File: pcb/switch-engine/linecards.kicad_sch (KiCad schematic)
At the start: 11 parts, among them J14 ARF6-08-S-D-A-K-TR, J15 ARF6-08-S-D-A-K-TR, J16 CONN_01X10, J17 ARF6-08-S-D-A-K-TR, J18 ARF6-08-S-D-A-K-TR, J19 CONN_01X10, U15 SIT9121AI-2BF-XXS156.250000G, U8 XILINX_ULTRASCALEPLUS_B676

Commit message: Continued initial schematic work on switch engine
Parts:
- added C104, C105, C106, C107, C108, C109, C110, C98: 0.47 uF, azonenberg_pcb:EIA_0402_CAP_NOSILK, symbol device:C
- added U18, U19, U20, U21: 74LVC1T45, azonenberg_pcb:DFN_6_0.5MM_1.6x1.6MM_TI_DPK, symbol special-azonenberg:74LVC1T45
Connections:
- net 2V5: now also C107.1, C108.1, C109.1, C110.1, U18.6 (VCCB), U19.6 (VCCB), U20.6 (VCCB), U21.6 (VCCB)
- net 3V3: now also C104.1, C105.1, C106.1, C98.1, U18.1 (VCCA), U19.1 (VCCA), U20.1 (VCCA), U21.1 (VCCA)
- net GND: now also C104.2, C105.2, C106.2, C107.2, C108.2, C109.2, C110.2, C98.2, U18.2 (GND), U19.2 (GND), U20.2 (GND), U21.2 (GND)
- net LC0_MDC: now also U20.4 (B)
- net LC0_MDC_3V3: now also U20.3 (A)
- net LC0_MDIO: now also U18.4 (B)
- net LC0_MDIO_3V3: now also U18.3 (A)
- net LC0_MDIO_OE: now also U18.5 (DIR)
- net LC1_MDC: now also U21.4 (B)
- net LC1_MDC_3V3: now also U21.3 (A)
- net LC1_MDIO: now also U19.4 (B)
- net LC1_MDIO_3V3: now also U19.3 (A)
- net LC1_MDIO_OE: now also U19.5 (DIR)
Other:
- note added: "MDIO/MDC to line cards are LVCMOS25 Everything else is LVCMOS33"
- note removed: "NOTE: MDIO/MDC to line cards are LVCMOS25 Everything else is LVCMOS33"

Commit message: First iteration of main board PCB schematic is now passing ERC
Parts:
- U8: value XILINX_ULTRASCALEPLUS_B676 -> XCKU5P-2FFVB676I
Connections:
- net 3V3: now also U20.5 (DIR), U21.5 (DIR)
- no-connect marks 24 -> 32
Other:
- company: (none) -> Antikernel Labs
- title: (none) -> LATENTRED Ethernet Switch - Main Board
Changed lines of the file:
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@@
 	(generator_version "8.0")
 	(paper "A3")
+	(title_block
+		(title "LATENTRED Ethernet Switch - Main Board")
+		(date "2025-06-02")
+		(rev "0.1")
+		(company "Antikernel Labs")
+		(comment 1 "Andrew D. Zonenberg")
+	)
 	(junction
 		(at 147.32 205.74)
@@
 	)
 	(no_connect
+		(at 64.77 241.3)
+	)
+	(no_connect
 		(at 39.37 187.96)
 	)
@@
 	)
 	(no_connect
+		(at 147.32 241.3)
+	)
+	(no_connect
+		(at 64.77 190.5)
+	)
+	(no_connect
 		(at 39.37 41.91)
 	)
@@
 	)
 	(no_connect
+		(at 147.32 243.84)
+	)
+	(no_connect
+		(at 147.32 190.5)
+	)
+	(no_connect
 		(at 201.93 193.04)
 	)
@@
 	)
 	(no_connect
+		(at 64.77 243.84)
+	)
+	(no_connect
 		(at 39.37 49.53)
 	)
@@
 	)
 	(no_connect
+		(at 147.32 187.96)
+	)
+	(no_connect
+		(at 64.77 187.96)
+	)
+	(no_connect
 		(at 39.37 241.3)
 	)
@@
 	(wire
 		(pts
+			(xy 298.45 74.93) (xy 298.45 77.47)
+		)
+		(stroke
+			(width 0)
+			(type default)
+		)
+	)
+	(wire
+		(pts
 			(xy 64.77 149.86) (xy 64.77 152.4)
 		)
@@
 	(wire
 		(pts
+			(xy 298.45 58.42) (xy 298.45 60.96)
+		)
+		(stroke
+			(width 0)
+			(type default)
+		)
+	)
+	(wire
+		(pts
 			(xy 121.92 210.82) (xy 121.92 213.36)
 		)
@@
 			)
 		)
-		(property "Value" "XILINX_ULTRASCALEPLUS_B676"
+		(property "Value" "XCKU5P-2FFVB676I"
 			(at 207.01 205.74 0)
 			(effects
@@
 			)
 		)
-		(property "Value" "XILINX_ULTRASCALEPLUS_B676"
+		(property "Value" "XCKU5P-2FFVB676I"
 			(at 207.01 125.73 0)
 			(effects
@@
 			)
 		)
-		(property "Value" "XILINX_ULTRASCALEPLUS_B676"
+		(property "Value" "XCKU5P-2FFVB676I"
 			(at 44.45 125.73 0)
 			(effects
@@
 			)
 		)
-		(property "Value" "XILINX_ULTRASCALEPLUS_B676"
+		(property "Value" "XCKU5P-2FFVB676I"
 			(at 125.73 125.73 0)
 			(effects

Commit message: Added footprints and created initial skeleton of layout
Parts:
- U8: footprint (none) -> azonenberg_pcb:BGA_676_27x27_FULLARRAY_1MM_FFG676
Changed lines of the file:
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@@
 			)
 		)
-		(property "Footprint" ""
+		(property "Footprint" "azonenberg_pcb:BGA_676_27x27_FULLARRAY_1MM_FFG676"
 			(at 270.51 200.66 0)
 			(effects
@@
 			)
 		)
-		(property "Footprint" ""
+		(property "Footprint" "azonenberg_pcb:BGA_676_27x27_FULLARRAY_1MM_FFG676"
 			(at 270.51 120.65 0)
 			(effects
@@
 			)
 		)
-		(property "Footprint" ""
+		(property "Footprint" "azonenberg_pcb:BGA_676_27x27_FULLARRAY_1MM_FFG676"
 			(at 107.95 120.65 0)
 			(effects
@@
 			)
 		)
-		(property "Footprint" ""
+		(property "Footprint" "azonenberg_pcb:BGA_676_27x27_FULLARRAY_1MM_FFG676"
 			(at 189.23 120.65 0)
 			(effects

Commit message: Lots of progress routing ARC6s
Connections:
- net LC0_PHY0_LANE0_TX_N: now also U8.AA5 (MGTYTXP0_225); no longer U8.AA4 (MGTYTXN0_225)
- net LC0_PHY0_LANE0_TX_P: now also U8.AA4 (MGTYTXN0_225); no longer U8.AA5 (MGTYTXP0_225)
- net LC0_PHY0_LANE1_TX_N: now also U8.W5 (MGTYTXP1_225); no longer U8.W4 (MGTYTXN1_225)
- net LC0_PHY0_LANE1_TX_P: now also U8.W4 (MGTYTXN1_225); no longer U8.W5 (MGTYTXP1_225)
- net LC0_PHY0_LANE2_RX_N: now also U8.T2 (MGTYRXP2_225); no longer U8.T1 (MGTYRXN2_225)
- net LC0_PHY0_LANE2_RX_P: now also U8.T1 (MGTYRXN2_225); no longer U8.T2 (MGTYRXP2_225)
- net LC0_PHY0_LANE2_TX_N: now also U8.U5 (MGTYTXP2_225); no longer U8.U4 (MGTYTXN2_225)
- net LC0_PHY0_LANE2_TX_P: now also U8.U4 (MGTYTXN2_225); no longer U8.U5 (MGTYTXP2_225)
- net LC0_PHY1_LANE0_TX_N: now also U8.R5 (MGTYTXP3_225); no longer U8.R4 (MGTYTXN3_225)
- net LC0_PHY1_LANE0_TX_P: now also U8.R4 (MGTYTXN3_225); no longer U8.R5 (MGTYTXP3_225)
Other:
- note added: "Polarity swap"
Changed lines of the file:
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@@
+		)
+	)
+	(text "Polarity swap"
+		(exclude_from_sim no)
+		(at 62.23 95.25 0)
+		(effects
+			(font
+				(size 1.27 1.27)
+			)
+			(justify left)
+		)
+	)
+	(text "Polarity swap"
+		(exclude_from_sim no)
+		(at 62.23 82.55 0)
+		(effects
+			(font
+				(size 1.27 1.27)
+			)
+			(justify left)
+		)
+	)
+	(text "Polarity swap"
+		(exclude_from_sim no)
+		(at 60.96 118.11 0)
+		(effects
+			(font
+				(size 1.27 1.27)
+			)
+			(justify left)
 		)
 	)
@@
 		)
 	)
+	(text "Polarity swap"
+		(exclude_from_sim no)
+		(at 62.23 102.87 0)
+		(effects
+			(font
+				(size 1.27 1.27)
+			)
+			(justify left)
+		)
+	)
 	(text "Line card 1"
 		(exclude_from_sim no)
@@
 		)
 	)
+	(text "Polarity swap"
+		(exclude_from_sim no)
+		(at 62.23 110.49 0)
+		(effects
+			(font
+				(size 1.27 1.27)
+			)
+			(justify left)
+		)
+	)
 	(label "LC0_PHY0_LANE2_RX_P"
-		(at 39.37 80.01 180)
+		(at 39.37 82.55 180)
 		(fields_autoplaced yes)
 		(effects
@@
 	)
 	(label "LC0_PHY0_LANE2_TX_N"
-		(at 39.37 113.03 180)
+		(at 39.37 110.49 180)
 		(fields_autoplaced yes)
 		(effects
@@
 	)
 	(label "LC0_PHY0_LANE1_TX_N"
-		(at 39.37 105.41 180)
+		(at 39.37 102.87 180)
 		(fields_autoplaced yes)
 		(effects
@@
 	)
 	(label "LC0_PHY0_LANE1_TX_P"
-		(at 39.37 102.87 180)
+		(at 39.37 105.41 180)
 		(fields_autoplaced yes)
 		(effects
@@
 	)
 	(label "LC0_PHY1_LANE0_TX_P"
-		(at 39.37 118.11 180)
+		(at 39.37 120.65 180)
 		(fields_autoplaced yes)
 		(effects
@@
 	)
 	(label "LC0_PHY0_LANE2_RX_N"
-		(at 39.37 82.55 180)
+		(at 39.37 80.01 180)
 		(fields_autoplaced yes)
 		(effects
@@
 	)
 	(label "LC0_PHY1_LANE0_TX_N"
-		(at 39.37 120.65 180)
+		(at 39.37 118.11 180)
 		(fields_autoplaced yes)
 		(effects
@@
 	)
 	(label "LC0_PHY0_LANE0_TX_N"
-		(at 39.37 97.79 180)
+		(at 39.37 95.25 180)
 		(fields_autoplaced yes)
 		(effects
@@
 	)
 	(label "LC0_PHY0_LANE2_TX_P"
-		(at 39.37 110.49 180)
+		(at 39.37 113.03 180)
 		(fields_autoplaced yes)
 		(effects
@@
 	)
 	(label "LC0_PHY0_LANE0_TX_P"
-		(at 39.37 95.25 180)
-		(fields_autoplaced yes)
-		(effects
+		(at 39.37 97.79 180)
+		(fields_autoplaced yes)
+		(effects

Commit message: Progress on GTY routing
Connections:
- net LC0_PHY1_LANE1_TX_N: now also U8.N5 (MGTYTXP0_226); no longer U8.N4 (MGTYTXN0_226)
- net LC0_PHY1_LANE1_TX_P: now also U8.N4 (MGTYTXN0_226); no longer U8.N5 (MGTYTXP0_226)
- net LC0_PHY1_LANE2_TX_N: now also U8.L5 (MGTYTXP1_226); no longer U8.L4 (MGTYTXN1_226)
- net LC0_PHY1_LANE2_TX_P: now also U8.L4 (MGTYTXN1_226); no longer U8.L5 (MGTYTXP1_226)
- net LC1_PHY0_LANE0_TX_N: now also U8.J5 (MGTYTXP2_226); no longer U8.J4 (MGTYTXN2_226)
- net LC1_PHY0_LANE0_TX_P: now also U8.J4 (MGTYTXN2_226); no longer U8.J5 (MGTYTXP2_226)
- net LC1_PHY0_LANE1_TX_N: now also U8.G5 (MGTYTXP3_226); no longer U8.G4 (MGTYTXN3_226)
- net LC1_PHY0_LANE1_TX_P: now also U8.G4 (MGTYTXN3_226); no longer U8.G5 (MGTYTXP3_226)
- net LC1_PHY0_LANE2_RX_N: now also U8.C3 (MGTYRXN1_227); no longer U8.D1 (MGTYRXN0_227)
- net LC1_PHY0_LANE2_RX_P: now also U8.C4 (MGTYRXP1_227); no longer U8.D2 (MGTYRXP0_227)
- net LC1_PHY0_LANE2_TX_N: now also U8.E5 (MGTYTXP1_227); no longer U8.F6 (MGTYTXN0_227)
- net LC1_PHY0_LANE2_TX_P: now also U8.E4 (MGTYTXN1_227); no longer U8.F7 (MGTYTXP0_227)
- net LC1_PHY1_LANE0_RX_N: now also U8.D1 (MGTYRXN0_227); no longer U8.C3 (MGTYRXN1_227)
- net LC1_PHY1_LANE0_RX_P: now also U8.D2 (MGTYRXP0_227); no longer U8.C4 (MGTYRXP1_227)
- net LC1_PHY1_LANE0_TX_N: now also U8.F6 (MGTYTXN0_227); no longer U8.E4 (MGTYTXN1_227)
- net LC1_PHY1_LANE0_TX_P: now also U8.F7 (MGTYTXP0_227); no longer U8.E5 (MGTYTXP1_227)
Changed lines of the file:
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@@
+		)
+	)
+	(text "Polarity swap"
+		(exclude_from_sim no)
+		(at 223.52 102.87 0)
+		(effects
+			(font
+				(size 1.27 1.27)
+			)
+			(justify left)
 		)
 	)
@@
 		)
 	)
+	(text "Polarity swap"
+		(exclude_from_sim no)
+		(at 142.24 110.49 0)
+		(effects
+			(font
+				(size 1.27 1.27)
+			)
+			(justify left)
+		)
+	)
 	(text "MDIO level shifters"
 		(exclude_from_sim no)
@@
 		)
 	)
+	(text "Polarity swap"
+		(exclude_from_sim no)
+		(at 142.24 95.25 0)
+		(effects
+			(font
+				(size 1.27 1.27)
+			)
+			(justify left)
+		)
+	)
 	(text "Low speed control buses"
 		(exclude_from_sim no)
@@
 		)
 	)
+	(text "Polarity swap"
+		(exclude_from_sim no)
+		(at 142.24 118.11 0)
+		(effects
+			(font
+				(size 1.27 1.27)
+			)
+			(justify left)
+		)
+	)
 	(text "Use ARC6-08-12.0-LU-LD-2-1 cable"
 		(exclude_from_sim no)
@@
 		)
 	)
+	(text "Polarity swap"
+		(exclude_from_sim no)
+		(at 142.24 102.87 0)
+		(effects
+			(font
+				(size 1.27 1.27)
+			)
+			(justify left)
+		)
+	)
 	(text "MDIO/MDC to line cards are LVCMOS25\nEverything else is LVCMOS33"
 		(exclude_from_sim no)
@@
 	)
 	(label "LC1_PHY1_LANE0_RX_P"
-		(at 201.93 72.39 180)
+		(at 201.93 64.77 180)
 		(fields_autoplaced yes)
 		(effects
@@
 	)
 	(label "LC1_PHY0_LANE0_TX_N"
-		(at 120.65 113.03 180)
+		(at 120.65 110.49 180)
 		(fields_autoplaced yes)
 		(effects
@@
 	)
 	(label "LC1_PHY0_LANE0_TX_P"
-		(at 120.65 110.49 180)
+		(at 120.65 113.03 180)
 		(fields_autoplaced yes)
 		(effects
@@
 	)
 	(label "LC1_PHY1_LANE0_TX_P"
-		(at 201.93 102.87 180)
+		(at 201.93 95.25 180)
 		(fields_autoplaced yes)
 		(effects
@@
 	)
 	(label "LC1_PHY0_LANE2_RX_P"
-		(at 201.93 64.77 180)
+		(at 201.93 72.39 180)
 		(fields_autoplaced yes)
 		(effects
@@
 	)
 	(label "LC1_PHY0_LANE1_TX_N"
-		(at 120.65 120.65 180)
+		(at 120.65 118.11 180)
 		(fields_autoplaced yes)
 		(effects
@@
 	)
 	(label "LC1_PHY0_LANE2_TX_N"
-		(at 201.93 97.79 180)
+		(at 201.93 102.87 180)
 		(fields_autoplaced yes)
 		(effects
@@
 	)
 	(label "LC1_PHY1_LANE0_RX_N"
-		(at 201.93 74.93 180)
+		(at 201.93 67.31 180)
 		(fields_autoplaced yes)
 		(effects
@@
 	)
 	(label "LC0_PHY1_LANE1_TX_N"
-		(at 120.65 97.79 180)
+		(at 120.65 95.25 180)
 		(fields_autoplaced yes)
 		(effects
@@
 	)
 	(label "LC0_PHY1_LANE2_TX_N"
-		(at 120.65 105.41 180)
+		(at 120.65 102.87 180)
 		(fields_autoplaced yes)
 		(effects
@@
 	)
 	(label "LC1_PHY0_LANE2_TX_P"
-		(at 201.93 95.25 180)
+		(at 201.93 105.41 180)
 		(fields_autoplaced yes)
 		(effects
@@
 	)
 	(label "LC1_PHY0_LANE1_TX_P"
-		(at 120.65 118.11 180)
+		(at 120.65 120.65 180)
 		(fields_autoplaced yes)
 		(effects
@@
 	)
 	(label "LC1_PHY0_LANE2_RX_N"
-		(at 201.93 67.31 180)
+		(at 201.93 74.93 180)
 		(fields_autoplaced yes)
 		(effects
@@
 	)
 	(label "LC0_PHY1_LANE1_TX_P"
-		(at 120.65 95.25 180)
+		(at 120.65 97.79 180)
 		(fields_autoplaced yes)
 		(effects
@@
 	)
 	(label "LC0_PHY1_LANE2_TX_P"
-		(at 120.65 102.87 180)
+		(at 120.65 105.41 180)
 		(fields_autoplaced yes)
 		(effects
@@
 	)
 	(label "LC1_PHY1_LANE0_TX_N"
-		(at 201.93 105.41 180)
-		(fields_autoplaced yes)
-		(effects
+		(at 201.93 97.79 180)
+		(fields_autoplaced yes)
+		(effects

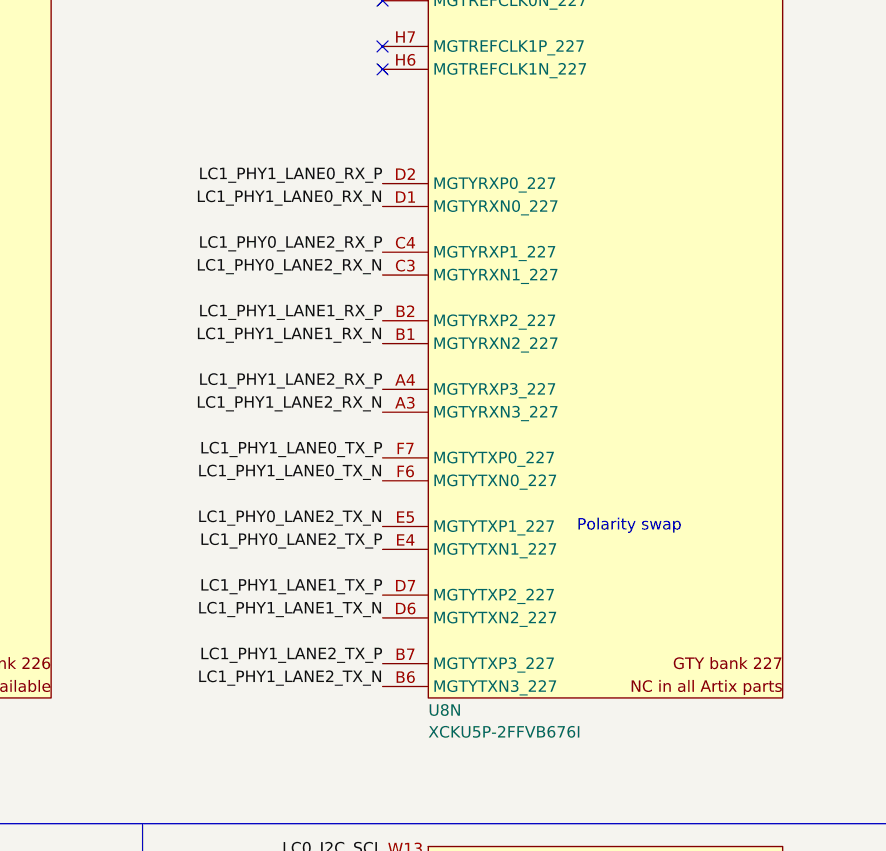
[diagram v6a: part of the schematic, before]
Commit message: More tweaking to SERDES routing
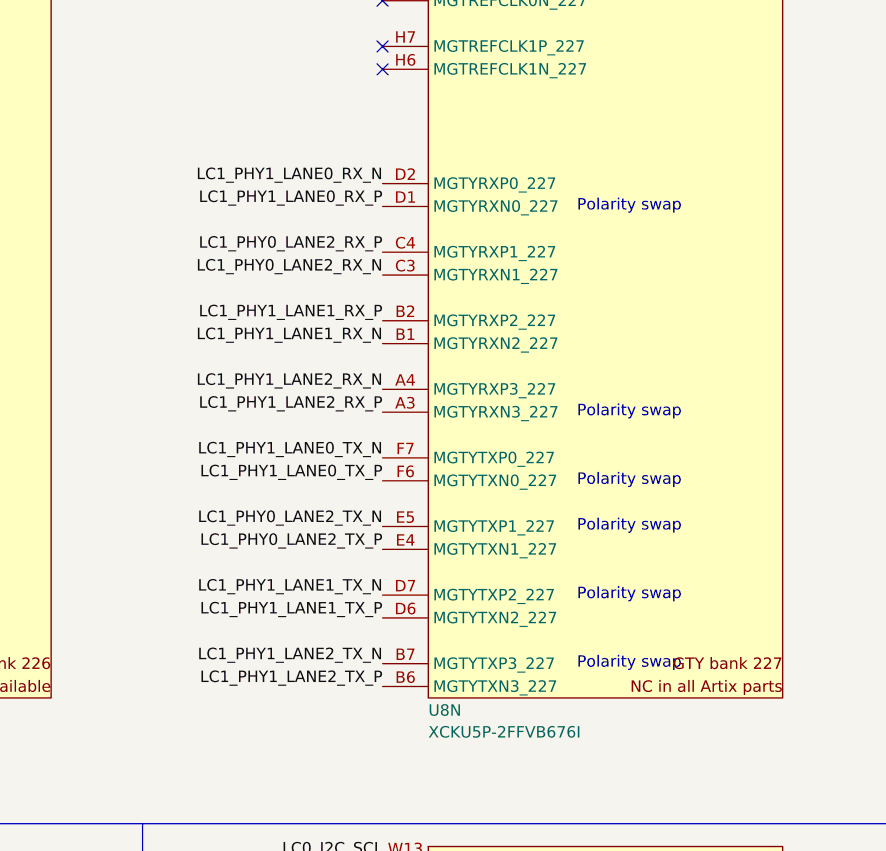
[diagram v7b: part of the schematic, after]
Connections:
- net LC1_PHY1_LANE0_RX_N: now also U8.D2 (MGTYRXP0_227); no longer U8.D1 (MGTYRXN0_227)
- net LC1_PHY1_LANE0_RX_P: now also U8.D1 (MGTYRXN0_227); no longer U8.D2 (MGTYRXP0_227)
- net LC1_PHY1_LANE0_TX_N: now also U8.F7 (MGTYTXP0_227); no longer U8.F6 (MGTYTXN0_227)
- net LC1_PHY1_LANE0_TX_P: now also U8.F6 (MGTYTXN0_227); no longer U8.F7 (MGTYTXP0_227)
- net LC1_PHY1_LANE1_TX_N: now also U8.D7 (MGTYTXP2_227); no longer U8.D6 (MGTYTXN2_227)
- net LC1_PHY1_LANE1_TX_P: now also U8.D6 (MGTYTXN2_227); no longer U8.D7 (MGTYTXP2_227)
- net LC1_PHY1_LANE2_RX_N: now also U8.A4 (MGTYRXP3_227); no longer U8.A3 (MGTYRXN3_227)
- net LC1_PHY1_LANE2_RX_P: now also U8.A3 (MGTYRXN3_227); no longer U8.A4 (MGTYRXP3_227)
- net LC1_PHY1_LANE2_TX_N: now also U8.B7 (MGTYTXP3_227); no longer U8.B6 (MGTYTXN3_227)
- net LC1_PHY1_LANE2_TX_P: now also U8.B6 (MGTYTXN3_227); no longer U8.B7 (MGTYTXP3_227)
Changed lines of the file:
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@@
+		)
+	)
+	(text "Polarity swap"
+		(exclude_from_sim no)
+		(at 223.52 67.31 0)
+		(effects
+			(font
+				(size 1.27 1.27)
+			)
+			(justify left)
 		)
 	)
@@
 	(text "Polarity swap"
 		(exclude_from_sim no)
+		(at 223.52 118.11 0)
+		(effects
+			(font
+				(size 1.27 1.27)
+			)
+			(justify left)
+		)
+	)
+	(text "Polarity swap"
+		(exclude_from_sim no)
 		(at 62.23 102.87 0)
+		(effects
+			(font
+				(size 1.27 1.27)
+			)
+			(justify left)
+		)
+	)
+	(text "Polarity swap"
+		(exclude_from_sim no)
+		(at 223.52 110.49 0)
 		(effects
 			(font
@@
 	(text "Polarity swap"
 		(exclude_from_sim no)
+		(at 223.52 90.17 0)
+		(effects
+			(font
+				(size 1.27 1.27)
+			)
+			(justify left)
+		)
+	)
+	(text "Polarity swap"
+		(exclude_from_sim no)
 		(at 142.24 118.11 0)
 		(effects
@@
 	(text "Polarity swap"
 		(exclude_from_sim no)
+		(at 223.52 97.79 0)
+		(effects
+			(font
+				(size 1.27 1.27)
+			)
+			(justify left)
+		)
+	)
+	(text "Polarity swap"
+		(exclude_from_sim no)
 		(at 142.24 102.87 0)
 		(effects
@@
 	)
 	(label "LC1_PHY1_LANE0_RX_P"
-		(at 201.93 64.77 180)
+		(at 201.93 67.31 180)
 		(fields_autoplaced yes)
 		(effects
@@
 	)
 	(label "LC1_PHY1_LANE2_TX_N"
-		(at 201.93 120.65 180)
+		(at 201.93 118.11 180)
 		(fields_autoplaced yes)
 		(effects
@@
 	)
 	(label "LC1_PHY1_LANE0_TX_P"
-		(at 201.93 95.25 180)
+		(at 201.93 97.79 180)
 		(fields_autoplaced yes)
 		(effects
@@
 	)
 	(label "LC1_PHY1_LANE0_RX_N"
-		(at 201.93 67.31 180)
+		(at 201.93 64.77 180)
 		(fields_autoplaced yes)
 		(effects
@@
 	)
 	(label "LC1_PHY1_LANE2_TX_P"
-		(at 201.93 118.11 180)
+		(at 201.93 120.65 180)
 		(fields_autoplaced yes)
 		(effects
@@
 	)
 	(label "LC1_PHY1_LANE2_RX_N"
-		(at 201.93 90.17 180)
+		(at 201.93 87.63 180)
 		(fields_autoplaced yes)
 		(effects
@@
 	)
 	(label "LC1_PHY1_LANE1_TX_P"
-		(at 201.93 110.49 180)
+		(at 201.93 113.03 180)
 		(fields_autoplaced yes)
 		(effects
@@
 	)
 	(label "LC1_PHY1_LANE1_TX_N"
-		(at 201.93 113.03 180)
+		(at 201.93 110.49 180)
 		(fields_autoplaced yes)
 		(effects
@@
 	)
 	(label "LC1_PHY1_LANE2_RX_P"
-		(at 201.93 87.63 180)
+		(at 201.93 90.17 180)
 		(fields_autoplaced yes)
 		(effects
@@
 	)
 	(label "LC1_PHY1_LANE0_TX_N"
-		(at 201.93 97.79 180)
-		(fields_autoplaced yes)
-		(effects
+		(at 201.93 95.25 180)
+		(fields_autoplaced yes)
+		(effects
